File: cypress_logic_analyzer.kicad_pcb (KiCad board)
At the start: 2 copper layers, 35.6 x 40.6 mm, 12 parts, among them P1 CONN_02X10, P2 CONN_02X10, P3 CONN_01X09, U1 74LCX245

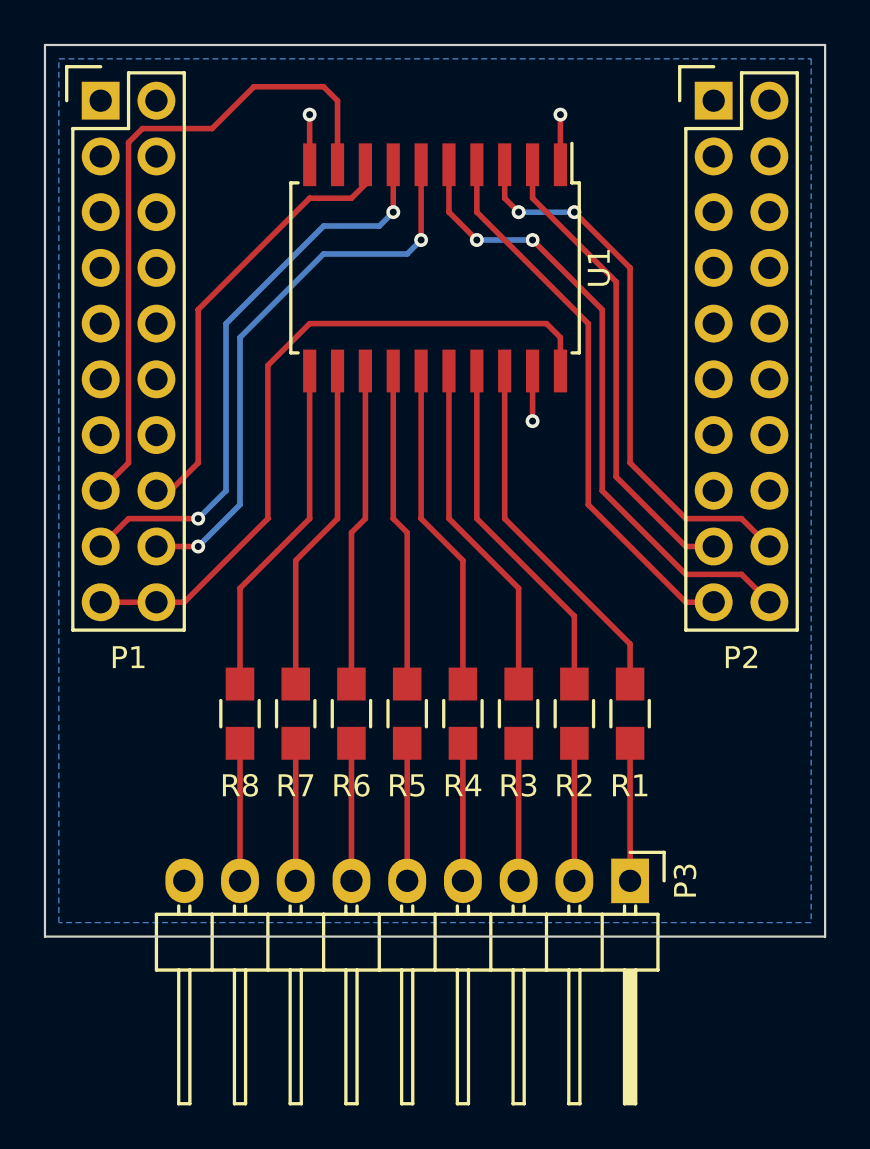
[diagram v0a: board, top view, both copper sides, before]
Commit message: Rev1.1, fixed routing, added decoupling cap
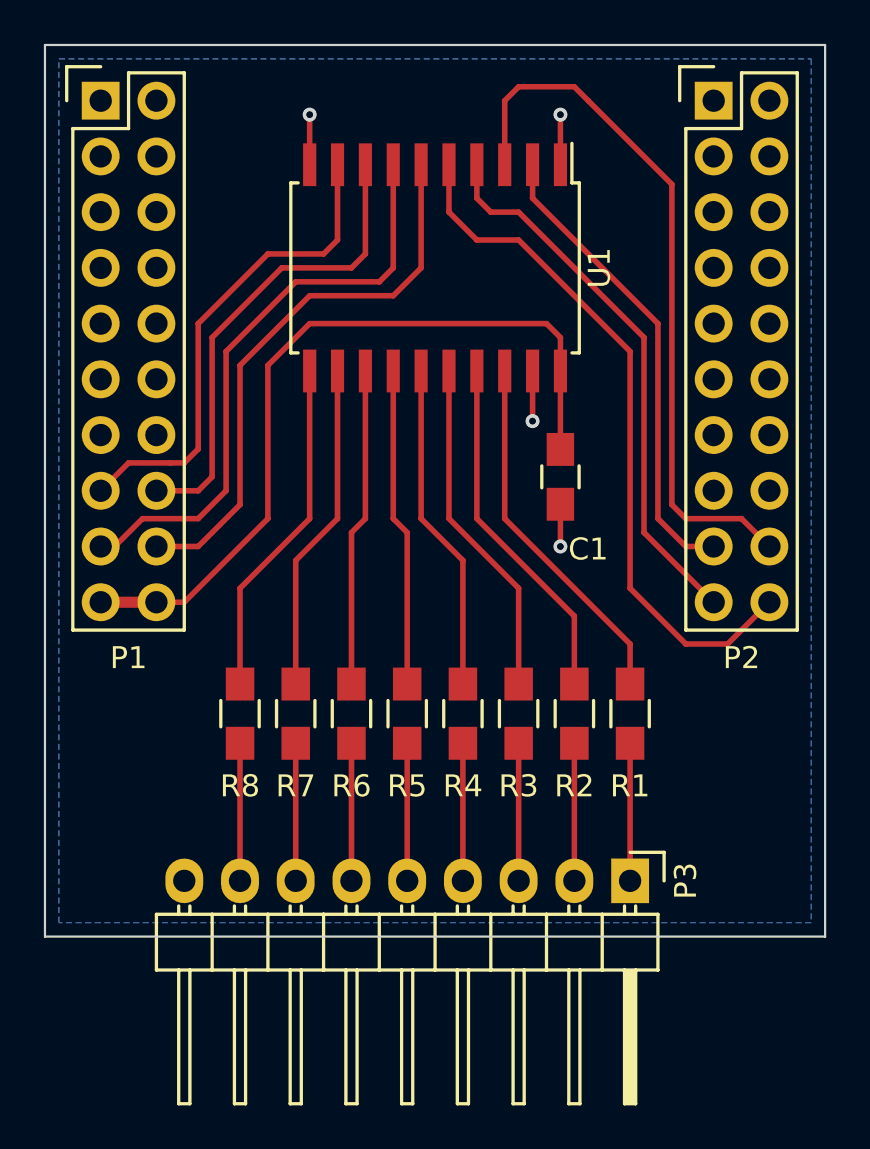
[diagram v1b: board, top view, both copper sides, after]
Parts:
- added C1: .1uF, Capacitors_SMD:C_0805_HandSoldering, F.Cu at (158.1, 107.3)
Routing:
- net /PB0: track 30.2 -> 22.3 mm
- net /PB6: track 25.4 -> 32.5 mm, vias 2 -> 0
- net VCC: track 32.1 -> 35.7 mm
- net /PB4: track 29.0 -> 32.0 mm, vias 2 -> 0
- net /PB1: track 20.3 -> 23.3 mm
- net GND: track 6.86 -> 8.78 mm, vias 3 -> 4
- net /PB2: track 26.3 -> 27.0 mm, vias 2 -> 0
- net /PB3: vias 2 -> 0
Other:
- board text added: "Cypress FX2 EZ-USB Logic Analyzer Buffer 1.1 @ExplodingLemur http://blog.explodinglemur.org https://github.com/ExplodingLemur/ezusb-logicanalyzer Creative Commons BY-SA"
- board text removed: "Cypress FX2 EZ-USB Logic Analyzer Buffer 1.0 @ExplodingLemur http://blog.explodinglemur.org https://github.com/ExplodingLemur/ezusb-logicanalyzer Creative Commons BY-SA"
